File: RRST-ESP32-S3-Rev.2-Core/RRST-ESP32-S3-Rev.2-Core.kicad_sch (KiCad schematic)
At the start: 34 parts, among them J1 Conn_01x22_Pin, J2 USB_C_Receptacle_USB2.0_16P, J3 Conn_01x22_Pin, J4 Conn_01x02_Pin, J5 Conn_01x04_Socket, J6 Conn_01x04_Socket, SW1 SW_Push, SW2 SW_Push, U1 ESP32-S3-WROOM-1, U2 LD1117S33TR_SOT223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

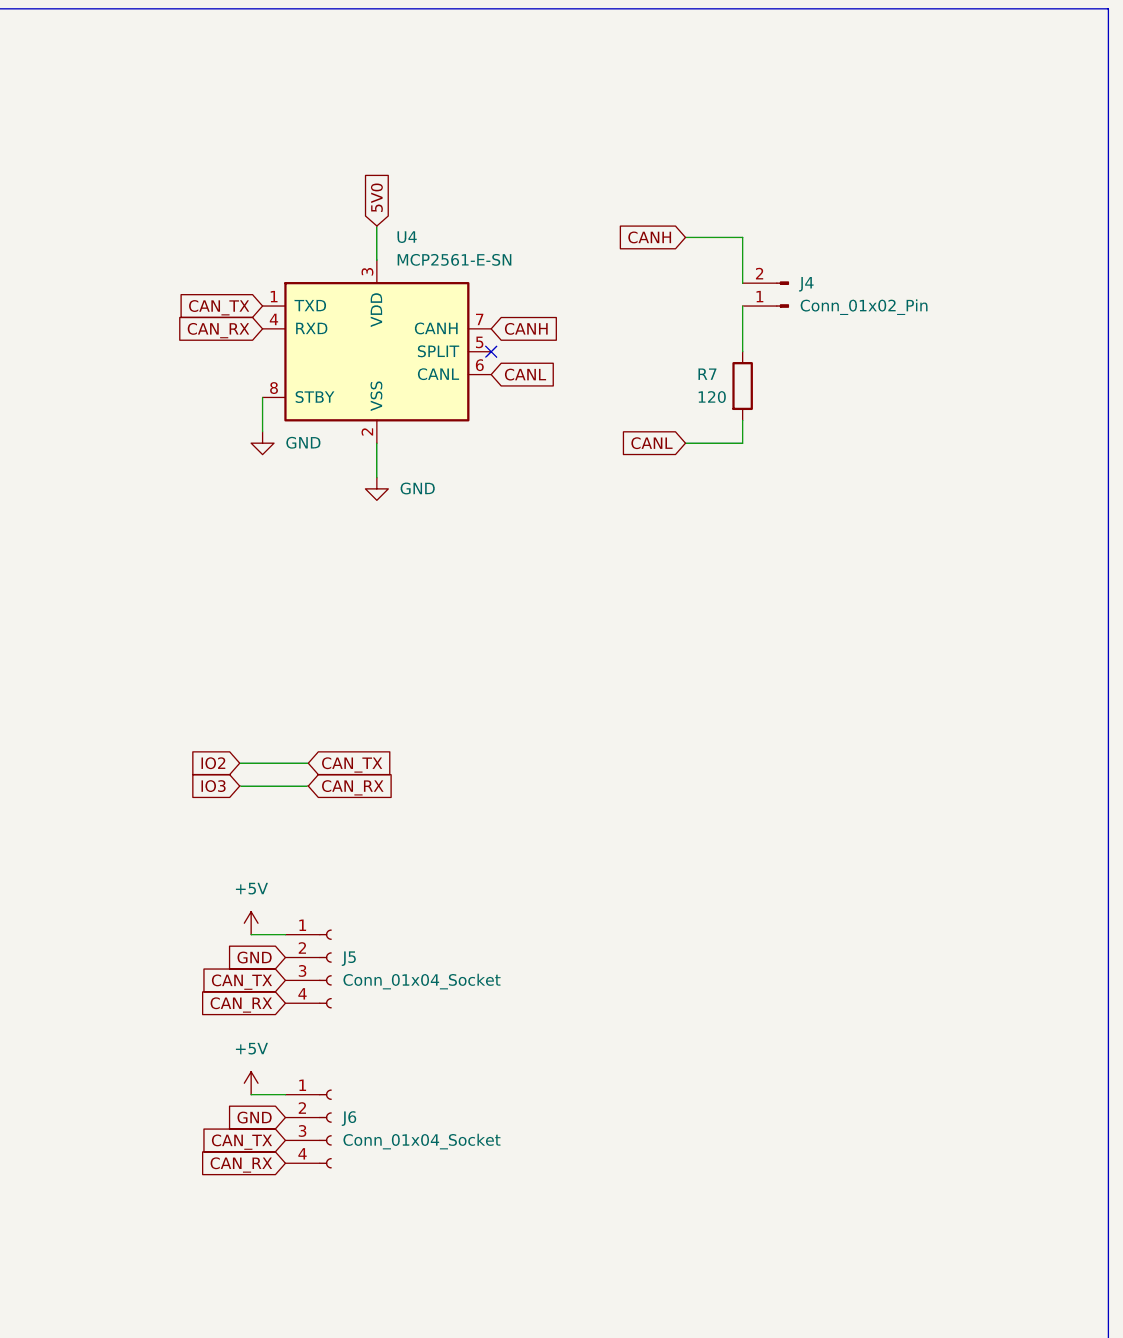
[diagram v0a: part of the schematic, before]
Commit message: 自動配線&未配線の手直し完了
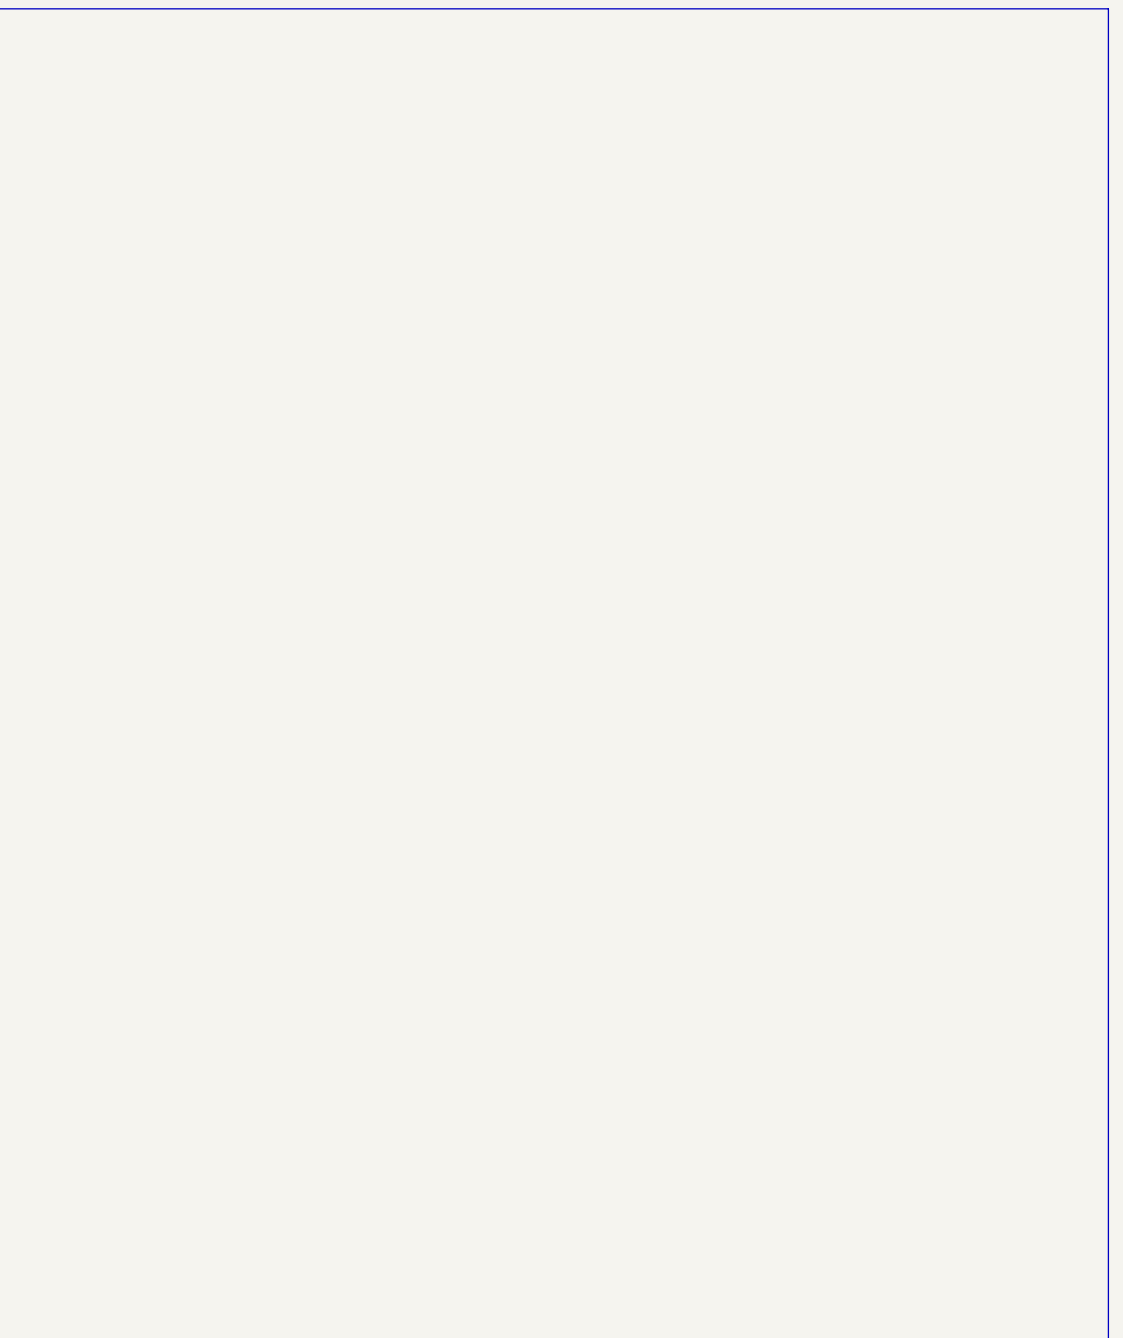
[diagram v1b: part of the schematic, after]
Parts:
- removed J4: Conn_01x02_Pin, Connector_PinHeader_2.54mm:PinHeader_1x02_P2.54mm_Vertical, symbol Connector:Conn_01x02_Pin
- removed J5, J6: Conn_01x04_Socket, Connector_JST:JST_XH_B4B-XH-A_1x04_P2.50mm_Vertical, symbol Connector:Conn_01x04_Socket
- removed R7: 120, Resistor_SMD:R_0603_1608Metric, symbol Device:R
- removed U4: MCP2561-E-SN, Package_SO:SOIC-8_3.9x4.9mm_P1.27mm, symbol Interface_CAN_LIN:MCP2561-E-SN
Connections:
- net CAN_RX renamed IO3
- net CAN_TX renamed IO2
- no-connect marks 4 -> 3
